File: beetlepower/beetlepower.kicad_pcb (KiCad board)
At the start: 2 copper layers, 43.5 x 29 mm, 14 parts, among them J1 Battery, J2 OUT2, J3 OUT3, J4 OUT4, J5 Conn_01x03_Male, U1 L7805

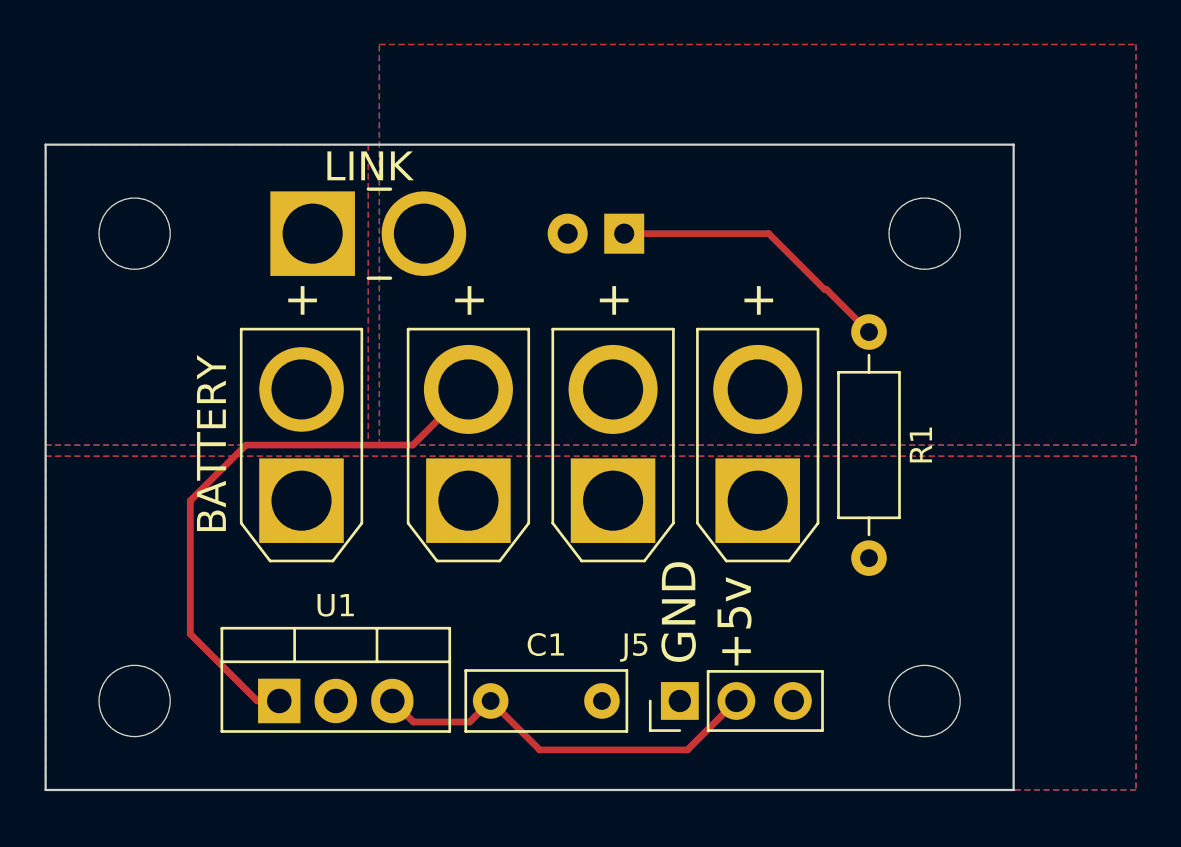
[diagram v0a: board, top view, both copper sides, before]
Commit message: PCBs for send off
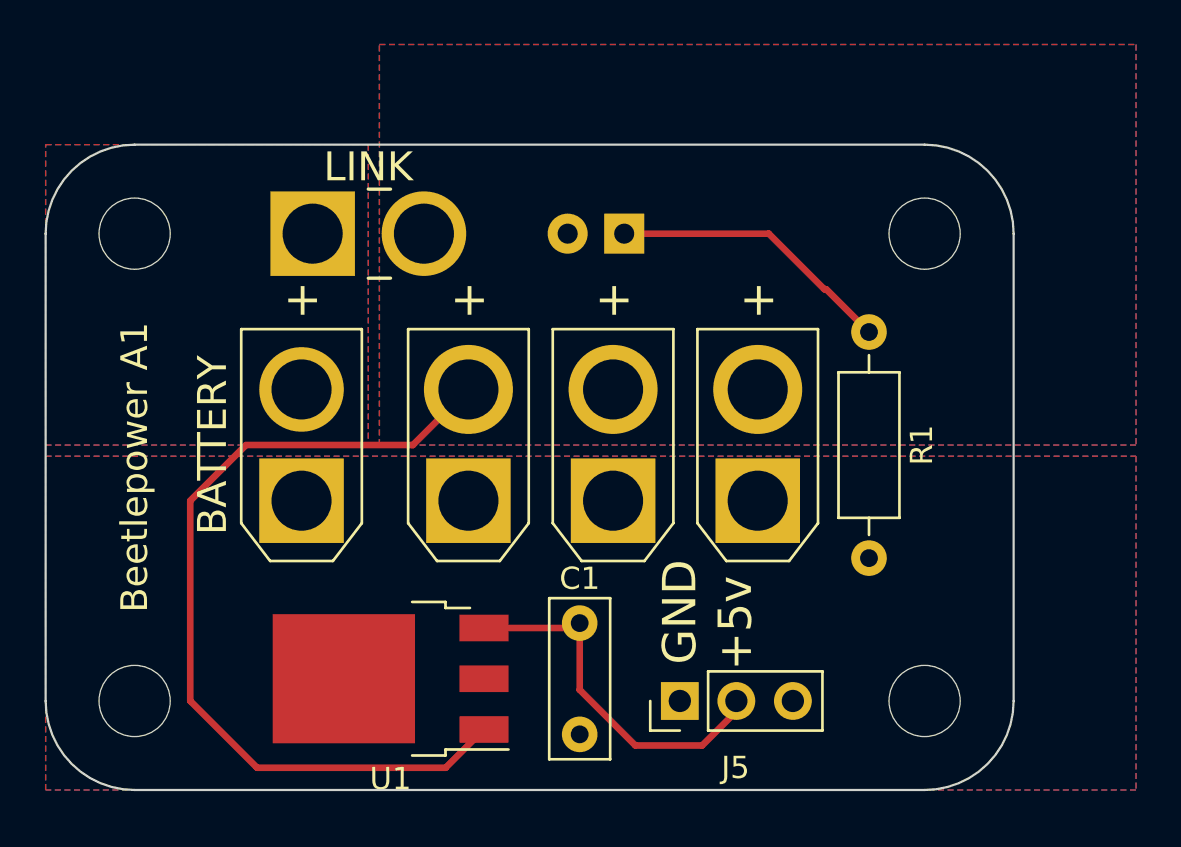
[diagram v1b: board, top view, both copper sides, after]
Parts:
- U1: value L7805 -> MC7805; footprint Package_TO_SOT_THT:TO-220-3_Vertical -> Package_TO_SOT_SMD:TO-252-3_TabPin2
- moved C1 5.32 mm to (105.0, 85.5), turned to -90 degrees
- moved U1 5.10 mm to (96.5, 88.0), turned to 180 degrees
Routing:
- net /B+: track 25.8 -> 38.7 mm
- net +5V: track 18.1 -> 16.6 mm
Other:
- outline, holes or cut-outs redrawn
- board text added: "Beetlepower A1"

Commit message: special footprints for pth+smd
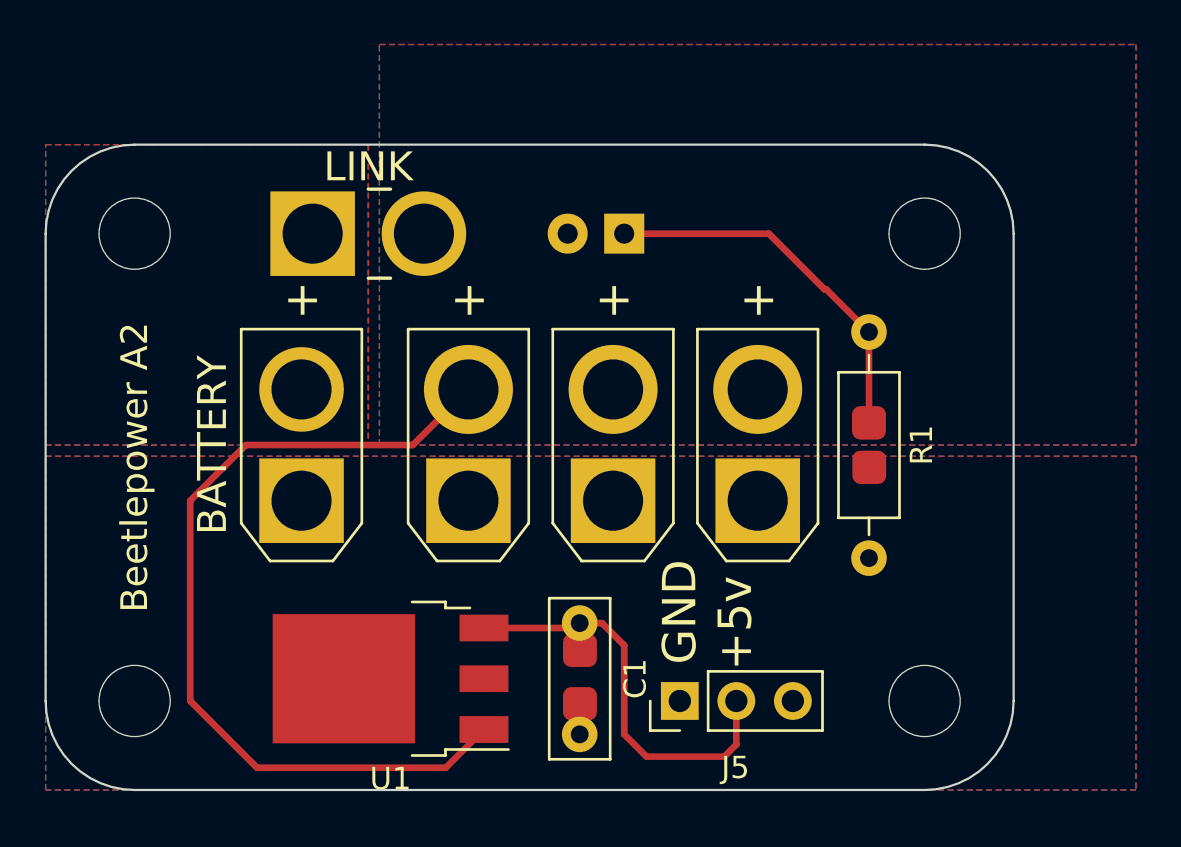
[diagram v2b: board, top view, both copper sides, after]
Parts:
- C1: footprint Capacitor_THT:C_Disc_D7.0mm_W2.5mm_P5.00mm -> beetlepower-xt30:C-pth-and-smd
- R1: footprint Resistor_THT:R_Axial_DIN0207_L6.3mm_D2.5mm_P10.16mm_Horizontal -> beetlepower-xt30:Resistor-pth-and-smd
- moved R1 5.08 mm to (118.0, 77.5)
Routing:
- net Net-(D1-Pad1): track 12.8 -> 16.9 mm
- net +5V: track 16.6 -> 18.4 mm
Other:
- board text added: "Beetlepower A2"
- board text removed: "Beetlepower A1"
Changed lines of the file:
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@@
     )
   )
-  (footprint "Resistor_THT:R_Axial_DIN0207_L6.3mm_D2.5mm_P10.16mm_Horizontal" (layer "F.Cu")
-    (at 118 72.42 -90)
+  (footprint "beetlepower-xt30:Resistor-pth-and-smd" (layer "F.Cu")
+    (at 118 77.5 -90)
     (descr "Resistor, Axial_DIN0207 series, Axial, Horizontal, pin pitch=10.16mm, 0.25W = 1/4W, length*diameter=6.3*2.5mm^2, http://cdn-reichelt.de/documents/datenblatt/B400/1_4W%23YAG.pdf")
     (tags "Resistor Axial_DIN0207 series Axial Horizontal pin pitch 10.16mm 0.25W = 1/4W length 6.3mm diameter 2.5mm")
@@
     (property "Sheetname" "")
     (attr through_hole)
-    (fp_text reference "R1" (at 5.08 -2.37 90) (layer "F.SilkS")
-      (effects (font (size 1 1) (thickness 0.15)))
-    )
-    (fp_text value "R" (at 5.08 2.37 90) (layer "F.Fab") hide
-      (effects (font (size 1 1) (thickness 0.15)))
-    )
-    (fp_text user "${REFERENCE}" (at 5.08 0 90) (layer "F.Fab") hide
-      (effects (font (size 1 1) (thickness 0.15)))
-    )
-    (fp_line (start 1.04 0) (end 1.81 0) (layer "F.SilkS") (width 0.12))
-    (fp_line (start 8.35 -1.37) (end 1.81 -1.37) (layer "F.SilkS") (width 0.12))
-    (fp_line (start 9.12 0) (end 8.35 0) (layer "F.SilkS") (width 0.12))
-    (fp_line (start 1.81 -1.37) (end 1.81 1.37) (layer "F.SilkS") (width 0.12))
-    (fp_line (start 8.35 1.37) (end 8.35 -1.37) (layer "F.SilkS") (width 0.12))
-    (fp_line (start 1.81 1.37) (end 8.35 1.37) (layer "F.SilkS") (width 0.12))
-    (fp_line (start 11.21 1.5) (end 11.21 -1.5) (layer "F.CrtYd") (width 0.05))
-    (fp_line (start -1.05 -1.5) (end -1.05 1.5) (layer "F.CrtYd") (width 0.05))
-    (fp_line (start 11.21 -1.5) (end -1.05 -1.5) (layer "F.CrtYd") (width 0.05))
-    (fp_line (start -1.05 1.5) (end 11.21 1.5) (layer "F.CrtYd") (width 0.05))
-    (fp_line (start 8.23 -1.25) (end 1.93 -1.25) (layer "F.Fab") (width 0.1))
-    (fp_line (start 1.93 -1.25) (end 1.93 1.25) (layer "F.Fab") (width 0.1))
-    (fp_line (start 0 0) (end 1.93 0) (layer "F.Fab") (width 0.1))
-    (fp_line (start 8.23 1.25) (end 8.23 -1.25) (layer "F.Fab") (width 0.1))
-    (fp_line (start 10.16 0) (end 8.23 0) (layer "F.Fab") (width 0.1))
-    (fp_line (start 1.93 1.25) (end 8.23 1.25) (layer "F.Fab") (width 0.1))
-    (pad "1" thru_hole circle locked (at 0 0 270) (size 1.6 1.6) (drill 0.8) (layers *.Cu *.Mask)
+    (fp_text reference "R1" (at 0 -2.37 -90) (layer "F.SilkS")
+      (effects (font (size 1 1) (thickness 0.15)))
+    )
+    (fp_text value "R" (at 0 2.37 -90) (layer "F.Fab")
+      (effects (font (size 1 1) (thickness 0.15)))
+    )
+    (fp_text user "${REFERENCE}" (at 0 0 -90) (layer "F.Fab")
+      (effects (font (size 1 1) (thickness 0.15)))
+    )
+    (fp_line (start 3.27 -1.37) (end -3.27 -1.37) (layer "F.SilkS") (width 0.12))
+    (fp_line (start 4.04 0) (end 3.27 0) (layer "F.SilkS") (width 0.12))
+    (fp_line (start -4.04 0) (end -3.27 0) (layer "F.SilkS") (width 0.12))
+    (fp_line (start 3.27 1.37) (end 3.27 -1.37) (layer "F.SilkS") (width 0.12))
+    (fp_line (start -3.27 -1.37) (end -3.27 1.37) (layer "F.SilkS") (width 0.12))
+    (fp_line (start -3.27 1.37) (end 3.27 1.37) (layer "F.SilkS") (width 0.12))
+    (fp_line (start 6.13 1.5) (end 6.13 -1.5) (layer "F.CrtYd") (width 0.05))
+    (fp_line (start 6.13 -1.5) (end -6.13 -1.5) (layer "F.CrtYd") (width 0.05))
+    (fp_line (start -6.13 -1.5) (end -6.13 1.5) (layer "F.CrtYd") (width 0.05))
+    (fp_line (start -6.13 1.5) (end 6.13 1.5) (layer "F.CrtYd") (width 0.05))
+    (fp_line (start 5.08 0) (end 3.15 0) (layer "F.Fab") (width 0.1))
+    (fp_line (start -5.08 0) (end -3.15 0) (layer "F.Fab") (width 0.1))
+    (fp_line (start 3.15 -1.25) (end -3.15 -1.25) (layer "F.Fab") (width 0.1))
+    (fp_line (start -3.15 1.25) (end 3.15 1.25) (layer "F.Fab") (width 0.1))
+    (fp_line (start 3.15 1.25) (end 3.15 -1.25) (layer "F.Fab") (width 0.1))
+    (fp_line (start -3.15 -1.25) (end -3.15 1.25) (layer "F.Fab") (width 0.1))
+    (pad "1" smd roundrect locked (at -1 0 270) (size 1.5 1.524) (layers "F.Cu" "F.Mask") (roundrect_rratio 0.25)
       (net 3 "Net-(D1-Pad1)") (pintype "passive"))
-    (pad "2" thru_hole oval locked (at 10.16 0 270) (size 1.6 1.6) (drill 0.8) (layers *.Cu *.Mask)
+    (pad "1" thru_hole circle locked (at -5.08 0 270) (size 1.6 1.6) (drill 0.8) (layers *.Cu *.Mask)
+      (net 3 "Net-(D1-Pad1)") (pintype "passive"))
+    (pad "2" smd roundrect locked (at 1 -0.012 270) (size 1.5 1.524) (layers "F.Cu" "F.Mask") (roundrect_rratio 0.25)
+      (net 4 "/GND") (pintype "passive"))
+    (pad "2" thru_hole oval locked (at 5.08 0 270) (size 1.6 1.6) (drill 0.8) (layers *.Cu *.Mask)
       (net 4 "/GND") (pintype "passive"))
     (model "${KICAD6_3DMODEL_DIR}/Resistor_THT.3dshapes/R_Axial_DIN0207_L6.3mm_D2.5mm_P10.16mm_Horizontal.wrl"
@@
     (pad "1" np_thru_hole circle locked (at 0 0) (size 3.2 3.2) (drill 3.2) (layers *.Cu *.Mask))
   )
-  (footprint "Capacitor_THT:C_Disc_D7.0mm_W2.5mm_P5.00mm" (layer "F.Cu")
+  (footprint "beetlepower-xt30:C-pth-and-smd" (layer "F.Cu")
     (at 105 85.5 -90)
     (descr "C, Disc series, Radial, pin pitch=5.00mm, , diameter*width=7*2.5mm^2, Capacitor, http://cdn-reichelt.de/documents/datenblatt/B300/DS_KERKO_TC.pdf")
@@
     (property "Sheetname" "")
     (attr through_hole)
-    (fp_text reference "C1" (at -2 0 180) (layer "F.SilkS")
-      (effects (font (size 1 1) (thickness 0.15)))
-    )
-    (fp_text value "C" (at 2.5 2.5 90) (layer "F.Fab")
-      (effects (font (size 1 1) (thickness 0.15)))
-    )
-    (fp_text user "${REFERENCE}" (at 2.5 0 90) (layer "F.Fab")
-      (effects (font (size 1 1) (thickness 0.15)))
-    )
+    (fp_text reference "C1" (at 2.5 -2.5 -90) (layer "F.SilkS")
+      (effects (font (size 1 1) (thickness 0.15)))
+    )
+    (fp_text value "C" (at 2.5 2.5 -90) (layer "F.Fab")
+      (effects (font (size 1 1) (thickness 0.15)))
+    )
+    (fp_text user "${REFERENCE}" (at 2.5 0 -90) (layer "F.Fab")
+      (effects (font (size 1 1) (thickness 0.15)))
+    )
+    (fp_line (start -1.12 -1.37) (end 6.12 -1.37) (layer "F.SilkS") (width 0.12))
     (fp_line (start 6.12 -1.37) (end 6.12 1.37) (layer "F.SilkS") (width 0.12))
+    (fp_line (start -1.12 -1.37) (end -1.12 1.37) (layer "F.SilkS") (width 0.12))
     (fp_line (start -1.12 1.37) (end 6.12 1.37) (layer "F.SilkS") (width 0.12))
-    (fp_line (start -1.12 -1.37) (end -1.12 1.37) (layer "F.SilkS") (width 0.12))
-    (fp_line (start -1.12 -1.37) (end 6.12 -1.37) (layer "F.SilkS") (width 0.12))
+    (fp_line (start -1.25 -1.5) (end -1.25 1.5) (layer "F.CrtYd") (width 0.05))
+    (fp_line (start 6.25 1.5) (end 6.25 -1.5) (layer "F.CrtYd") (width 0.05))
+    (fp_line (start -1.25 1.5) (end 6.25 1.5) (layer "F.CrtYd") (width 0.05))
     (fp_line (start 6.25 -1.5) (end -1.25 -1.5) (layer "F.CrtYd") (width 0.05))
-    (fp_line (start 6.25 1.5) (end 6.25 -1.5) (layer "F.CrtYd") (width 0.05))
-    (fp_line (start -1.25 -1.5) (end -1.25 1.5) (layer "F.CrtYd") (width 0.05))
-    (fp_line (start -1.25 1.5) (end 6.25 1.5) (layer "F.CrtYd") (width 0.05))
-    (fp_line (start 6 -1.25) (end -1 -1.25) (layer "F.Fab") (width 0.1))
     (fp_line (start -1 -1.25) (end -1 1.25) (layer "F.Fab") (width 0.1))
     (fp_line (start -1 1.25) (end 6 1.25) (layer "F.Fab") (width 0.1))
+    (fp_line (start 6 -1.25) (end -1 -1.25) (layer "F.Fab") (width 0.1))
     (fp_line (start 6 1.25) (end 6 -1.25) (layer "F.Fab") (width 0.1))
+    (pad "1" smd roundrect locked (at 1.225 -0.012 270) (size 1.5 1.524) (layers "F.Cu" "F.Mask") (roundrect_rratio 0.25)
+      (net 5 "+5V") (pintype "passive"))
     (pad "1" thru_hole circle locked (at 0 0 270) (size 1.6 1.6) (drill 0.8) (layers *.Cu *.Mask)
       (net 5 "+5V") (pintype "passive"))
     (pad "2" thru_hole circle locked (at 5 0 270) (size 1.6 1.6) (drill 0.8) (layers *.Cu *.Mask)
+      (net 4 "/GND") (pintype "passive"))
+    (pad "2" smd roundrect locked (at 3.625 -0.012 270) (size 1.5 1.524) (layers "F.Cu" "F.Mask") (roundrect_rratio 0.25)
       (net 4 "/GND") (pintype "passive"))
     (model "${KICAD6_3DMODEL_DIR}/Capacitor_THT.3dshapes/C_Disc_D7.0mm_W2.5mm_P5.00mm.wrl"
@@
     (effects (font (size 1.3 1.3) (thickness 0.15)))
   )
-  (gr_text "Beetlepower A1" (at 85 78.5 90) (layer "F.SilkS")
+  (gr_text "Beetlepower A2" (at 85 78.5 90) (layer "F.SilkS")
     (effects (font (size 1.2 1.2) (thickness 0.15)))
   )
@@
   (segment (start 116 70.5) (end 116.08 70.5) (width 0.3) (layer "F.Cu") (net 3))
   (segment (start 107 68) (end 113.5 68) (width 0.3) (layer "F.Cu") (net 3))
+  (segment (start 118 76.5) (end 118 72.42) (width 0.3) (layer "F.Cu") (net 3))
   (segment (start 116.08 70.5) (end 118 72.42) (width 0.3) (layer "F.Cu") (net 3))
   (segment (start 104.78 85.72) (end 105 85.5) (width 0.3) (layer "F.Cu") (net 5))
-  (segment (start 112.04 89.46) (end 112.04 89) (width 0.3) (layer "F.Cu") (net 5))
-  (segment (start 105 88.5) (end 107.5 91) (width 0.3) (layer "F.Cu") (net 5))
-  (segment (start 105 85.5) (end 105 88.5) (width 0.3) (layer "F.Cu") (net 5))
-  (segment (start 107.5 91) (end 110.5 91) (width 0.3) (layer "F.Cu") (net 5))
+  (segment (start 106 85.5) (end 107 86.5) (width 0.3) (layer "F.Cu") (net 5))
+  (segment (start 111.5 91.5) (end 108 91.5) (width 0.3) (layer "F.Cu") (net 5))
+  (segment (start 107 86.5) (end 107 90.5) (width 0.3) (layer "F.Cu") (net 5))
+  (segment (start 112.04 90.96) (end 111.5 91.5) (width 0.3) (layer "F.Cu") (net 5))
+  (segment (start 112.04 89) (end 112.04 90.96) (width 0.3) (layer "F.Cu") (net 5))
+  (segment (start 108 91.5) (end 107 90.5) (width 0.3) (layer "F.Cu") (net 5))
   (segment (start 100.7 85.72) (end 104.78 85.72) (width 0.3) (layer "F.Cu") (net 5))
-  (segment (start 110.5 91) (end 112.04 89.46) (width 0.3) (layer "F.Cu") (net 5))
+  (segment (start 105 85.5) (end 106 85.5) (width 0.3) (layer "F.Cu") (net 5))
   (zone (net 1) (net_name "/B+IN") (layers F&B.Cu) (hatch edge 0.508)
     (connect_pads (clearance 0.25))
